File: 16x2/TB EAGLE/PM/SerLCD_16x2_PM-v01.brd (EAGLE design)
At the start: 73.7 x 99.1 mm, 5 parts

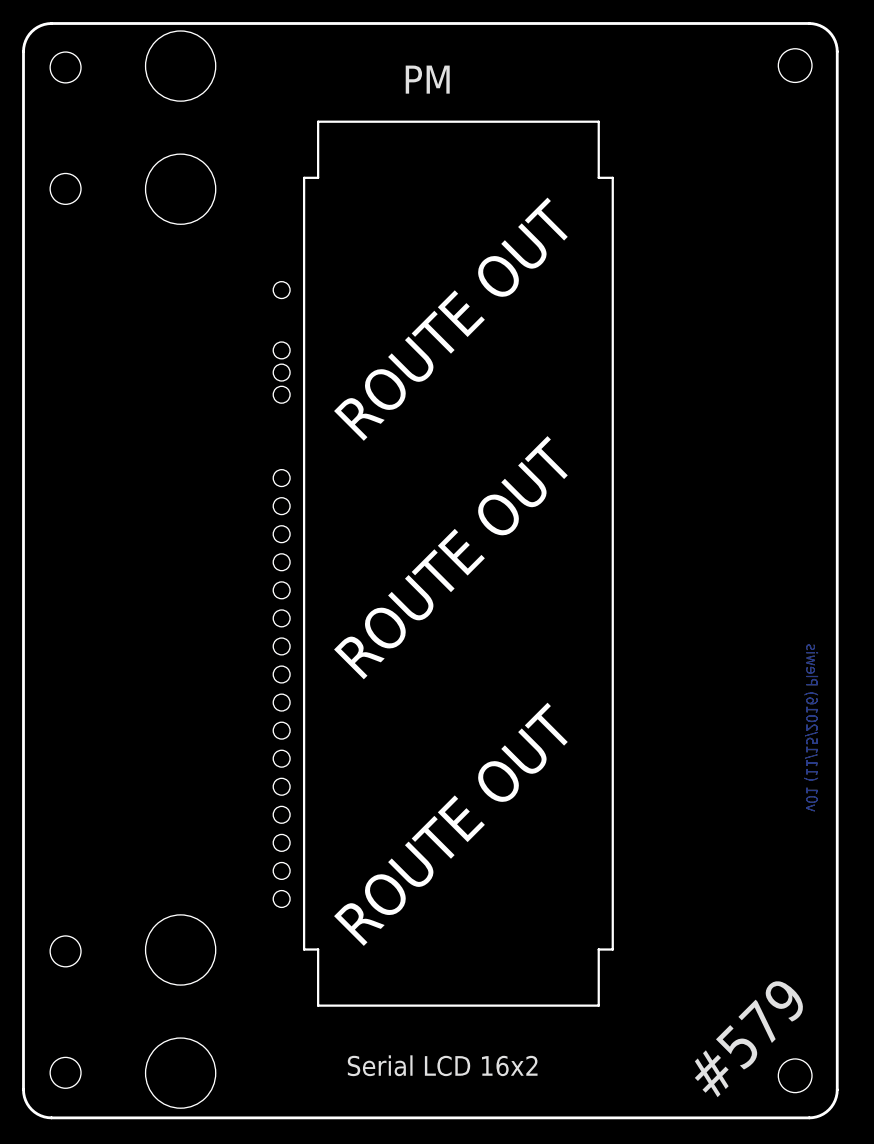
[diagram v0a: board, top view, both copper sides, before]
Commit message: Prepped 16x4_PM for acrylic - drills to 55mils
also moved "route out" text to tplace

also created dxf file for lazering
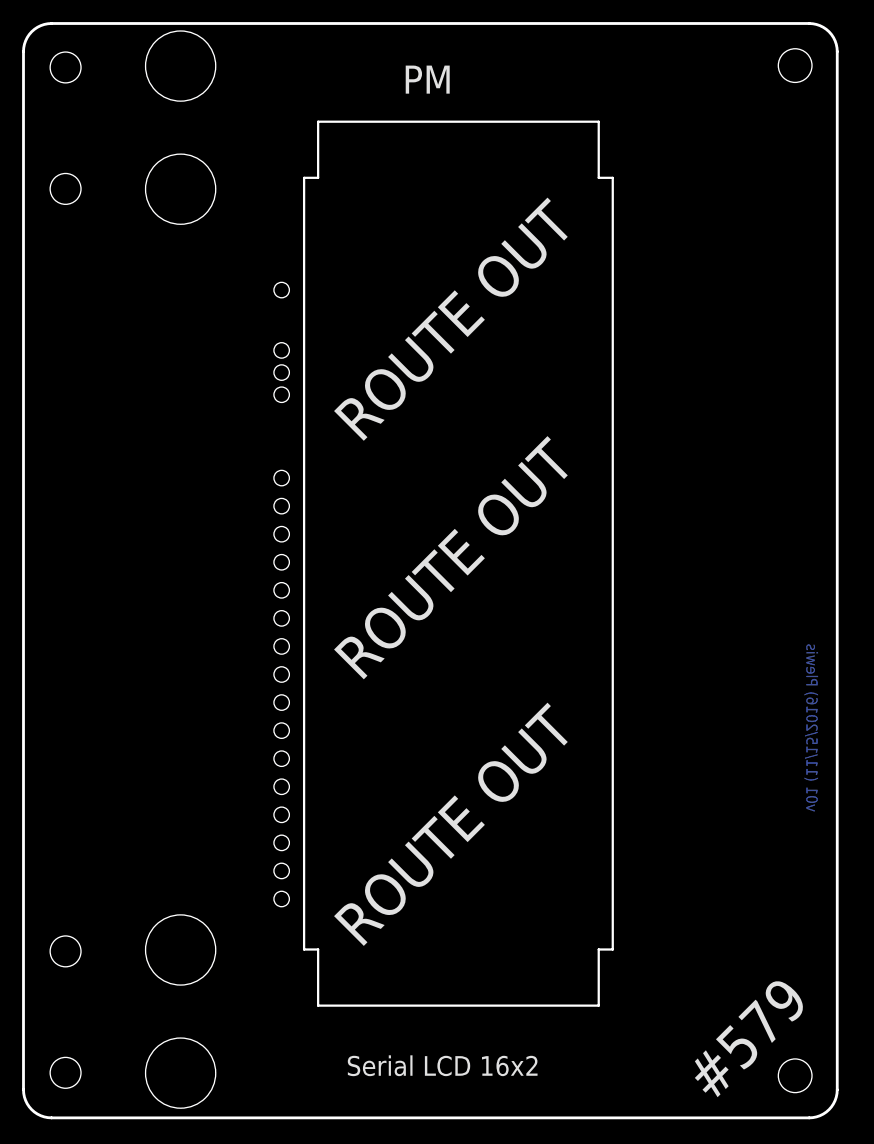
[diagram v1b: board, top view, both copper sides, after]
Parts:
- renumbered U$1 to U$2
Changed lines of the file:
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@@
 <grid distance="0.05" unitdist="inch" unit="inch" style="lines" multiple="1" display="yes" altdistance="0.005" altunitdist="inch" altunit="inch"/>
 <layers>
-<layer number="1" name="Top" color="4" fill="1" visible="yes" active="yes"/>
+<layer number="1" name="Top" color="4" fill="1" visible="no" active="yes"/>
 <layer number="2" name="Route2" color="1" fill="3" visible="no" active="no"/>
 <layer number="3" name="Route3" color="4" fill="3" visible="no" active="no"/>
@@
 <layer number="14" name="Route14" color="1" fill="6" visible="no" active="no"/>
 <layer number="15" name="Route15" color="4" fill="6" visible="no" active="no"/>
-<layer number="16" name="Bottom" color="1" fill="1" visible="yes" active="yes"/>
-<layer number="17" name="Pads" color="2" fill="1" visible="yes" active="yes"/>
-<layer number="18" name="Vias" color="2" fill="1" visible="yes" active="yes"/>
-<layer number="19" name="Unrouted" color="6" fill="1" visible="yes" active="yes"/>
+<layer number="16" name="Bottom" color="1" fill="1" visible="no" active="yes"/>
+<layer number="17" name="Pads" color="2" fill="1" visible="no" active="yes"/>
+<layer number="18" name="Vias" color="2" fill="1" visible="no" active="yes"/>
+<layer number="19" name="Unrouted" color="6" fill="1" visible="no" active="yes"/>
 <layer number="20" name="Dimension" color="15" fill="1" visible="yes" active="yes"/>
-<layer number="21" name="tPlace" color="16" fill="1" visible="yes" active="yes"/>
-<layer number="22" name="bPlace" color="14" fill="1" visible="yes" active="yes"/>
-<layer number="23" name="tOrigins" color="15" fill="1" visible="yes" active="yes"/>
-<layer number="24" name="bOrigins" color="15" fill="1" visible="yes" active="yes"/>
+<layer number="21" name="tPlace" color="16" fill="1" visible="no" active="yes"/>
+<layer number="22" name="bPlace" color="14" fill="1" visible="no" active="yes"/>
+<layer number="23" name="tOrigins" color="15" fill="1" visible="no" active="yes"/>
+<layer number="24" name="bOrigins" color="15" fill="1" visible="no" active="yes"/>
 <layer number="25" name="tNames" color="7" fill="1" visible="no" active="yes"/>
 <layer number="26" name="bNames" color="7" fill="1" visible="no" active="yes"/>
@@
 <layer number="43" name="vRestrict" color="2" fill="10" visible="no" active="yes"/>
 <layer number="44" name="Drills" color="7" fill="1" visible="no" active="yes"/>
-<layer number="45" name="Holes" color="7" fill="1" visible="yes" active="yes"/>
+<layer number="45" name="Holes" color="7" fill="1" visible="no" active="yes"/>
 <layer number="46" name="Milling" color="3" fill="1" visible="no" active="yes"/>
 <layer number="47" name="Measures" color="7" fill="1" visible="no" active="yes"/>
 <layer number="48" name="Document" color="7" fill="1" visible="no" active="yes"/>
-<layer number="49" name="Reference" color="13" fill="1" visible="yes" active="yes"/>
+<layer number="49" name="Reference" color="13" fill="1" visible="no" active="yes"/>
 <layer number="50" name="dxf" color="7" fill="1" visible="no" active="yes"/>
-<layer number="51" name="tDocu" color="6" fill="1" visible="yes" active="yes"/>
+<layer number="51" name="tDocu" color="6" fill="1" visible="no" active="yes"/>
 <layer number="52" name="bDocu" color="7" fill="1" visible="no" active="yes"/>
 <layer number="53" name="tGND_GNDA" color="7" fill="9" visible="no" active="no"/>
@@
 <wire x1="53.34" y1="85.09" x2="52.07" y2="85.09" width="0.2032" layer="20"/>
 <wire x1="52.07" y1="85.09" x2="52.07" y2="90.17" width="0.2032" layer="20"/>
-<text x="30.48" y="60.96" size="3.81" layer="20" font="vector" ratio="15" rot="R45">ROUTE OUT</text>
-<text x="30.48" y="39.37" size="3.81" layer="20" font="vector" ratio="15" rot="R45">ROUTE OUT</text>
-<text x="30.48" y="15.24" size="3.81" layer="20" font="vector" ratio="15" rot="R45">ROUTE OUT</text>
+<text x="30.48" y="60.96" size="3.81" layer="21" font="vector" ratio="15" rot="R45">ROUTE OUT</text>
+<text x="30.48" y="39.37" size="3.81" layer="21" font="vector" ratio="15" rot="R45">ROUTE OUT</text>
+<text x="30.48" y="15.24" size="3.81" layer="21" font="vector" ratio="15" rot="R45">ROUTE OUT</text>
 </plain>
 <attributes>
@@
 <element name="U$6" library="Testing" package="GOLD_HINGE_PM" value="GOLD_HINDGEPM+PF" x="0" y="80.01"/>
 <element name="U$7" library="Testing" package="GOLD_HINGE_PM" value="GOLD_HINDGEPM+PF" x="0" y="0"/>
-<element name="U$1" library="SerLCD_dimensions" package="SER_LCD_16X2_PM" value="" x="57.15" y="10.16" rot="R90"/>
+<element name="U$2" library="SerLCD_dimensions" package="SER_LCD_16X2_PM" value="" x="57.15" y="10.16" rot="R90"/>
 </elements>
 <signals>
